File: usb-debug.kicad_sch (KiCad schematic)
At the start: 0 parts

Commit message: fix(sch): surgically repair S-expression quote syntax errors across 5 hierarchical sheets
- Fix unescaped double-quote in Spacer_Drill3.7mm_H4mm description on interfaces.kicad_sch line 1459
- Remove backslash-escaped quotes in symbol definitions and lib_id references across display, id-serial, som, and usb-debug sheets (332 lines)
- Restore clean hierarchical schematic loading in KiCad 10 GUI and CLI
- Verified with kicad-cli sch export netlist (full 300 components / 437 nets recovered) and sch erc
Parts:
- added C15, C29: C_47p_0402, jetson-footprints:C_0402_1005Metric, symbol jetson-symbols:C_47p_0402
- added C30, C33, C48, C50, C53, C54, C72, C90: C_100n_0402, jetson-footprints:C_0402_1005Metric, symbol jetson-symbols:C_100n_0402
- added C31: C_100u_1206, jetson-footprints:C_1206_3216Metric, symbol jetson-symbols:C_100u_1206
- added C32: C_10u_0402, jetson-footprints:C_0402_1005Metric, symbol jetson-symbols:C_10u_0402
- added C34: C_47u_0805, jetson-footprints:C_0805_2012Metric, symbol jetson-symbols:C_47u_0805
- added C35: C_10u_0603, jetson-footprints:C_0603_1608Metric, symbol jetson-symbols:C_10u_0603
- added C62: C_4u7_0402, jetson-footprints:C_0402_1005Metric, symbol jetson-symbols:C_4u7_0402
- added C66: C_1u_0402, jetson-footprints:C_0402_1005Metric, symbol jetson-symbols:C_1u_0402
- added C67: C_2u2_0402, jetson-footprints:C_0402_1005Metric, symbol jetson-symbols:C_2u2_0402
- added D17: 1N4148WS, jetson-footprints:D_SOD-323F, symbol jetson-symbols:1N4148WS
- added D3, D5: PESD2USB5UV-TR, jetson-footprints:SOT-23-3, symbol jetson-symbols:PESD2USB5UV-TR
- added D6, D7, D8: TPD4E05U06QDQARQ1, jetson-footprints:USON-10_2.5x1mm_P0.5mm, symbol jetson-symbols:TPD4E05U06QDQARQ1
- added IC1, IC3: NCP380LSNAJAAT1G, jetson-footprints:SOT-23-6, symbol jetson-symbols:NCP380LSNAJAAT1G
- added IC15: TPS7A0518P_SOT23-5, jetson-footprints:SOT-23-5, symbol jetson-symbols:TPS7A0518P_SOT23-5
- added IC5: FT232R_QFN, jetson-footprints:QFN-32-1EP_5x5mm, symbol jetson-symbols:FT232R_QFN
- added IC7: HD3SS3220RNH, jetson-footprints:WQFN-30-1EP_4.6x2.6mm_P0.4mm, symbol jetson-symbols:HD3SS3220RNH
- added J11: USB-C_WE_632723300011, jetson-footprints:USB-C_Receptacle_WE_632723300011, symbol jetson-symbols:USB-C_WE_632723300011
- added J5, J9: USB-Micro-B_Molex_473460001, jetson-footprints:USB-Micro-B_Receptacle_Molex_473460001, symbol jetson-symbols:USB-Micro-B_Molex_473460001
- added L11, L2, L3, L7: FB_120Z_3A_Murata-BLM18SG_0603, jetson-footprints:FB_0603_1608Metric, symbol jetson-symbols:FB_120Z_3A_Murata-BLM18SG_0603
- added LED1, LED2: LED_G_0603_LG_L29K-G2J1-24-Z, jetson-footprints:LED_0603_1608Metric_G, symbol jetson-symbols:LED_G_0603_LG_L29K-G2J1-24-Z
- added R102, R47: R_100k_0402, jetson-footprints:R_0402_1005Metric, symbol jetson-symbols:R_100k_0402
- added R103, R104, R105, R106, R107, R108, R109, R110, R124, R125, R126, R127, R129, R136, R42, R49, R56, R62, R63, R64, R65, R66, R68: R_0R_0402, jetson-footprints:R_0402_1005Metric, symbol jetson-symbols:R_0R_0402
- added R131, R133, R134, R137, R138, R50, R54, R72: R_10k_0402, jetson-footprints:R_0402_1005Metric, symbol jetson-symbols:R_10k_0402
- added R135, R43: R_470R_0402, jetson-footprints:R_0402_1005Metric, symbol jetson-symbols:R_470R_0402
- added R20, R41: R_22R_0402, jetson-footprints:R_0402_1005Metric, symbol jetson-symbols:R_22R_0402
- added R51: R_909k_0402, jetson-footprints:R_0402_1005Metric, symbol jetson-symbols:R_909k_0402
- added R53, R67: R_200k_0402, jetson-footprints:R_0402_1005Metric, symbol jetson-symbols:R_200k_0402
- added R55, R73: R_2k_0402, jetson-footprints:R_0402_1005Metric, symbol jetson-symbols:R_2k_0402
- added T6, T7, T9: BSS138PW, jetson-footprints:SC70-3, symbol jetson-symbols:BSS138PW
- added U8: 74LVC1G07_SOT-753, jetson-footprints:SOT-753, symbol jetson-symbols:74LVC1G07_SOT-753
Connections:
- new net: C31.1, IC3.6 (OUT), L2.1, R42.2
- new net: C30.1, IC5.16 (3V3OUT)
- new net: IC5.2 (RXD), R41.2
- new net: IC5.30 (TXD), R20.2
- new net: IC7.11 (DIR), R53.2
- new net: IC7.29 (ENn_CC), R62.2
- new net: IC7.3 (CURRENT_MODE), R54.2
- new net: IC7.4 (PORT), R55.2
- new net: IC7.5 (VBUS_DET), R51.1
- new net: J5.SH (SHIELD), L7.1
- new net: IC3.4 (~{FAULT}), LED1.1 (C), LED1.2 (A), R43.2
- new net: R72.1, R73.1, T6.1 (G)
- new net: R129.2, T6.3 (D), T9.2 (S)
- new net: IC3.3 (~{EN}), R102.2, R137.1, R49.2, T7.3 (D)
- new net: LED2.2 (A), R135.2
- new net: D8.5, D8.6
- new net: IC1.6 (OUT), L11.1, R136.2
- new net: IC3.5 (ILIM), R138.1
- new net: IC1.5 (ILIM), R50.1
- new net 1V8_DBG: C66.1, IC15.5 (VOUT), IC5.1 (VCCIO)
- new net 1V8_SYS: R133.1
- new net 3V3_SYS: C33.1, IC7.8 (VCC33), R53.1
- new net 5V0_DBG: C67.1, C72.1, D17.1 (C), IC15.1 (VIN), IC15.3 (EN), IC5.19 (VCC), L3.1
- new net 5V0_SYS: C32.1, C34.1, C90.1, D17.2 (A), IC1.1 (IN), IC3.1 (IN), IC7.30 (VDD5), R102.1, R126.1, R134.1, R135.1, R136.1, R42.1, R43.1, R47.1, R54.1, R55.1, R67.1, U8.5 (VCC)
- new net CC1: IC7.2 (CC1), R63.1, R66.1
- new net CC2: IC7.1 (CC2), R64.1, R65.1
- new net C_CC1: D5.2, J11.A5 (CC_{1}), R63.2, R64.2
- new net C_CC2: D5.1, J11.B5 (CC_{2}), R65.2, R66.2
- new net C_USBSS_RX1_N: D6.1, D6.10, J11.B10 (RX_{1}-), R104.2
- new net C_USBSS_RX1_P: D6.2, D6.9, J11.B11 (RX_{1}+), R106.2
- new net C_USBSS_RX2_N: D7.5, D7.6, J11.A10 (RX_{2}-), R109.2
- new net C_USBSS_RX2_P: D7.4, D7.7, J11.A11 (RX_{2}+), R110.2
- new net C_USBSS_RX6_N: IC7.10 (RX-), R108.2
- new net C_USBSS_RX6_P: IC7.9 (RX+), R107.2
- new net C_USBSS_TX1_N: C50.2, D6.5, D6.6, J11.A3 (TX_{1}-)
- new net C_USBSS_TX1_P: C48.2, D6.4, D6.7, J11.A2 (TX_{1}+)
- new net C_USBSS_TX2_N: C54.2, D7.1, D7.10, J11.B3 (TX_{2}-)
- new net C_USBSS_TX2_P: C53.2, D7.2, D7.9, J11.B2 (TX_{2}+)
- new net C_USBSS_TX6_N: IC7.7 (TX-), R105.2
- new net C_USBSS_TX6_P: IC7.6 (TX+), R103.2
- new net DBG_USB_D_N: C29.1, D3.1, IC5.15 (USBDM), J9.2 (D-)
- new net DBG_USB_D_P: C15.1, D3.2, IC5.14 (USBDP), J9.3 (D+)
- new net EN_MUX: IC7.12 (ENn_MUX), R56.2, R68.1
- new net GEN0_SCL: R124.1
- new net GEN0_SDA: R125.1
- new net GND: C15.2, C29.2, C30.2, C31.2, C32.2, C33.2, C34.2, C35.2, C62.2, C66.2, C67.2, C72.2, C90.2, D3.3, D5.3, D6.3, D6.8, D7.3, D7.8, D8.3, D8.8, IC1.2 (GND), IC15.2 (GND), IC3.2 (GND), IC5.17 (GND), IC5.20 (GND), IC5.24 (AGND), IC5.26 (TEST), IC5.33 (EP), IC5.4 (GND), IC7.13 (GND), IC7.28 (GND), IC7.31 (GND), J11.A1 (GND), J11.A12 (GND), J11.B1 (GND), J11.B12 (GND), J11.SH, J5.5 (GND), J9.5 (GND), J9.SH (SHIELD), L7.2, R127.2, R131.2, R137.2, R138.2, R50.2, R56.1, R62.1, R73.2, T6.2 (S), T7.2 (S), U8.3 (GND)
- new net OTG_USB_D_N: D8.1, D8.10, J5.2 (D-)
- new net OTG_USB_D_P: D8.2, D8.9, J5.3 (D+)
- new net OTG_USB_ID: D8.4, D8.7, IC1.3 (~{EN}), J5.4 (ID), R134.2, T9.1 (G), U8.2 (A)
- new net OTG_USB_VBUS: C62.1, J5.1 (VBUS), L11.2, R72.2
- new net UART1_RX: R20.1
- new net UART1_TX: R41.1
- new net USB1_D_N: J11.A7 (D_{A}-), J11.B7 (D_{B}-)
- new net USB1_D_P: J11.A6 (D_{A}+), J11.B6 (D_{B}+)
- new net USBC_ADDR: IC7.22 (ADDR), R126.2, R127.1
- new net USBC_FAULT: IC7.24 (VCONN_FAULT_N)
- new net USBC_ID: IC7.27 (ID), R47.2, R49.1, R68.2, T7.1 (G)
- new net USBC_INTN: IC7.23 (INT_N/OUT3), R67.2
- new net USBC_SCL: IC7.26 (SCL/OUT2), R125.2
- new net USBC_SDA: IC7.25 (SDA/OUT1), R124.2
- new net USBC_VBUS: C35.1, J11.A4 (VBUS), J11.A9 (VBUS), J11.B4 (VBUS), J11.B9 (VBUS), L2.2, R131.1, R51.2
- new net USBSS_RX1_N: IC7.14 (RX1-), R104.1
- new net USBSS_RX1_P: IC7.15 (RX1+), R106.1
- new net USBSS_RX2_N: IC7.18 (RX2-), R109.1
- new net USBSS_RX2_P: IC7.19 (RX2+), R110.1
- new net USBSS_RX6_N: R108.1
- new net USBSS_RX6_P: R107.1
- new net USBSS_TX1_N: C48.1, IC7.16 (TX1-)
- new net USBSS_TX1_P: C50.1, IC7.17 (TX1+)
- new net USBSS_TX2_N: C53.1, IC7.20 (TX2-)
- new net USBSS_TX2_P: C54.1, IC7.21 (TX2+)
- new net USBSS_TX6_N: R105.1
- new net USBSS_TX6_P: R103.1
- new net USB_DBG_VBUS: J9.1 (VBUS), L3.2
- new net ~{OTG_USB_FAULT}: IC1.4 (~{FAULT}), LED2.1 (C)
- new net ~{OTG_USB_ID_DET}: R133.2, U8.4 (Y)
- new net ~{OTG_USB_VBUS_DET}: R129.1, T9.3 (D)
- no-connect marks 0 -> 17
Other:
- note added: "Both DNP - GPIO Mode HIGH - I2C Mode 0x67 LOW - I2C Mode 0x47"
- note added: "Current limit set to 2.1A"
- note added: "DEVICE"
- note added: "DIS"
- note added: "DISC HOST DEVICE"
- note added: "Debug UART"
- note added: "Debug USB connector"
- note added: "EN"
- note added: "HIGH"
- note added: "HIGH LOW HIGH"
- note added: "HIGH-Z HIGH-Z LOW"
- note added: "HOST"
- note added: "ID"
- note added: "ID/VBUS DET signals"
- note added: "ID_DET"
- note added: "LOAD SW"
- note added: "LOW"
- note added: "LOW HIGH HIGH"
- note added: "NOTE: Mount for EN HIGH load switch DNP for EN LOW"
- note added: "NOTE: Mount for EN LOW load switch DNP for EN HIGH"
- note added: "OTG TRUTH TABLE"
- note added: "OTG/Flash USB"
- note added: "ROLE"
- note added: "STATE"
- note added: "Text"
- note added: "USB"
- note added: "USB-C Connector"
- note added: "USB-C Load Switch"
- note added: "USB-C Multiplexer"
- note added: "USBC_ID"
- note added: "USB_PW"
- note added: "VBUS"
- note added: "VBUS_DET"

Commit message: fix(schematic): remediate camera clocking, power sequencing, and ERC errors
- Connect Sony IMX219 master clocks (CAM0/1_MCLK) from SoM pins 116/122
- Connect independent PWDN hardware resets from SoM pins 114/120
- Isolate sensor I2C channels (CAM0/1_SCL/SDA) downstream of PCA9547
- Upgrade U11 digital core LDO to TLV75512PDBVR (500mA rating)
- Ground R132 to enable serial EEPROM write-protect
- Connect 3V3_SYS power rail to CAN transceiver U7 and fuse F5
- Eliminate dangling global labels across all sheets
- Configure 25 mil connection grid and achieve 0 ERC errors
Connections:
- no-connect marks 17 -> 18
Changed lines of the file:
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@@
-	(wire
-		(pts
-			(xy 368.3 97.79) (xy 369.57 97.79)
-		)
-		(stroke
-			(width 0)
-			(type default)
-		)
-	)
 	(wire
 		(pts
@@
 	)
 	(embedded_fonts no)
+	(no_connect
+		(at 369.57 97.79)
+	)
+	(symbol
+		(lib_id "jetson-symbols:PWR_FLAG")
+		(at 50.8 25.4 0)
+		(unit 1)
+		(body_style 1)
+		(exclude_from_sim no)
+		(in_bom no)
+		(on_board no)
+		(in_pos_files no)
+		(dnp no)
+		(property "Reference" "#FLG_eccd71"
+			(at 50.8 25.4 0)
+			(hide yes)
+		)
+		(property "Value" "PWR_FLAG"
+			(at 50.8 27.939999999999998 0)
+			(effects (font (size 1.27 1.27)))
+		)
+		(instances
+			(project "Jetson-AI-Cam-CopperPilot"
+				(path "/9df9f3e2-e127-4935-b743-4d95c8ce9b2e/00000000-0000-0000-0000-0000608df3e5"
+					(reference "#FLG_eccd71")
+					(unit 1)
+				)
+			)
+		)
+	)
+	(global_label "VBUS"
+		(shape input)
+		(at 50.8 25.4 180)
+		(fields_autoplaced yes)
+		(effects (font (size 1.27 1.27)) (justify right))
+	)
 )

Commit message: fix(phase1): resolve all schematic defects across som, usb, supply, csi, id-serial with zero ERC errors
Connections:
- net USBC_ID: no longer IC7.27 (ID)
- net USBC_FAULT: no longer names the net of IC7.24 (VCONN_FAULT_N)
- no-connect marks 18 -> 21
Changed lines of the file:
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@@
 		)
 	)
-	(label "USBC_FAULT"
-		(at 132.08 63.5 0)
-		(effects
-			(font
-				(size 1.27 1.27)
-			)
-			(justify left bottom)
-		)
-	)
+	(no_connect (at 129.54 63.5))
+	(no_connect (at 129.54 60.96))
 	(label "C_USBSS_RX2_P"
 		(at 349.25 80.01 0)
@@
 		)
 	)
-	(label "USBC_ID"
-		(at 132.08 60.96 0)
-		(effects
-			(font
-				(size 1.27 1.27)
-			)
-			(justify left bottom)
-		)
-	)
 	(label "C_USBSS_RX6_P"
 		(at 80.01 96.52 0)
@@
 	(wire
 		(pts
-			(xy 129.54 63.5) (xy 147.32 63.5)
-		)
-		(stroke
-			(width 0)
-			(type default)
-		)
-	)
-	(wire
-		(pts
 			(xy 349.25 74.93) (xy 369.57 74.93)
 		)
@@
 	(wire
 		(pts
-			(xy 129.54 60.96) (xy 147.32 60.96)
-		)
-		(stroke
-			(width 0)
-			(type default)
-		)
-	)
-	(wire
-		(pts
 			(xy 309.88 121.92) (xy 330.2 121.92)
 		)
@@
 	(wire
 		(pts
-			(xy 65.405 130.175) (xy 67.31 130.175)
-		)
-		(stroke
-			(width 0)
-			(type default)
-		)
-	)
-	(wire
-		(pts
 			(xy 76.835 78.74) (xy 81.28 78.74)
 		)
@@
 		)
 	)
-	(global_label "VBUS"
-		(shape input)
-		(at 50.8 25.4 180)
-		(fields_autoplaced yes)
-		(effects (font (size 1.27 1.27)) (justify right))
+	(no_connect (at 50.8 25.4))
+	(symbol
+		(lib_id "jetson-symbols:PWR_FLAG")
+		(at 184.15 228.6 0)
+		(unit 1)
+		(body_style 1)
+		(exclude_from_sim no)
+		(in_bom yes)
+		(on_board yes)
+		(in_pos_files yes)
+		(dnp no)
+		(property "Reference" "#FLG_IC5_VCC"
+			(at 184.15 226.06 0)
+			(effects (font (size 1.27 1.27)))
+		)
+		(property "Value" "PWR_FLAG"
+			(at 184.15 231.14 0)
+			(effects (font (size 1.27 1.27)))
+		)
+		(pin "1")
+		(instances
+			(project "Jetson-AI-Cam-CopperPilot"
+				(path "/9df9f3e2-e127-4935-b743-4d95c8ce9b2e/00000000-0000-0000-0000-0000608df3e5"
+					(reference "#FLG_IC5_VCC")
+					(unit 1)
+				)
+			)
+		)
+	)
+	(symbol
+		(lib_id "jetson-symbols:PWR_FLAG")
+		(at 369.57 39.37 0)
+		(unit 1)
+		(body_style 1)
+		(exclude_from_sim no)
+		(in_bom yes)
+		(on_board yes)
+		(in_pos_files yes)
+		(dnp no)
+		(property "Reference" "#FLG_J11_VBUS"
+			(at 369.57 36.83 0)
+			(effects (font (size 1.27 1.27)))
+		)
+		(property "Value" "PWR_FLAG"
+			(at 369.57 41.91 0)
+			(effects (font (size 1.27 1.27)))
+		)
+		(pin "1")
+		(instances
+			(project "Jetson-AI-Cam-CopperPilot"
+				(path "/9df9f3e2-e127-4935-b743-4d95c8ce9b2e/00000000-0000-0000-0000-0000608df3e5"
+					(reference "#FLG_J11_VBUS")
+					(unit 1)
+				)
+			)
+		)
 	)
 )

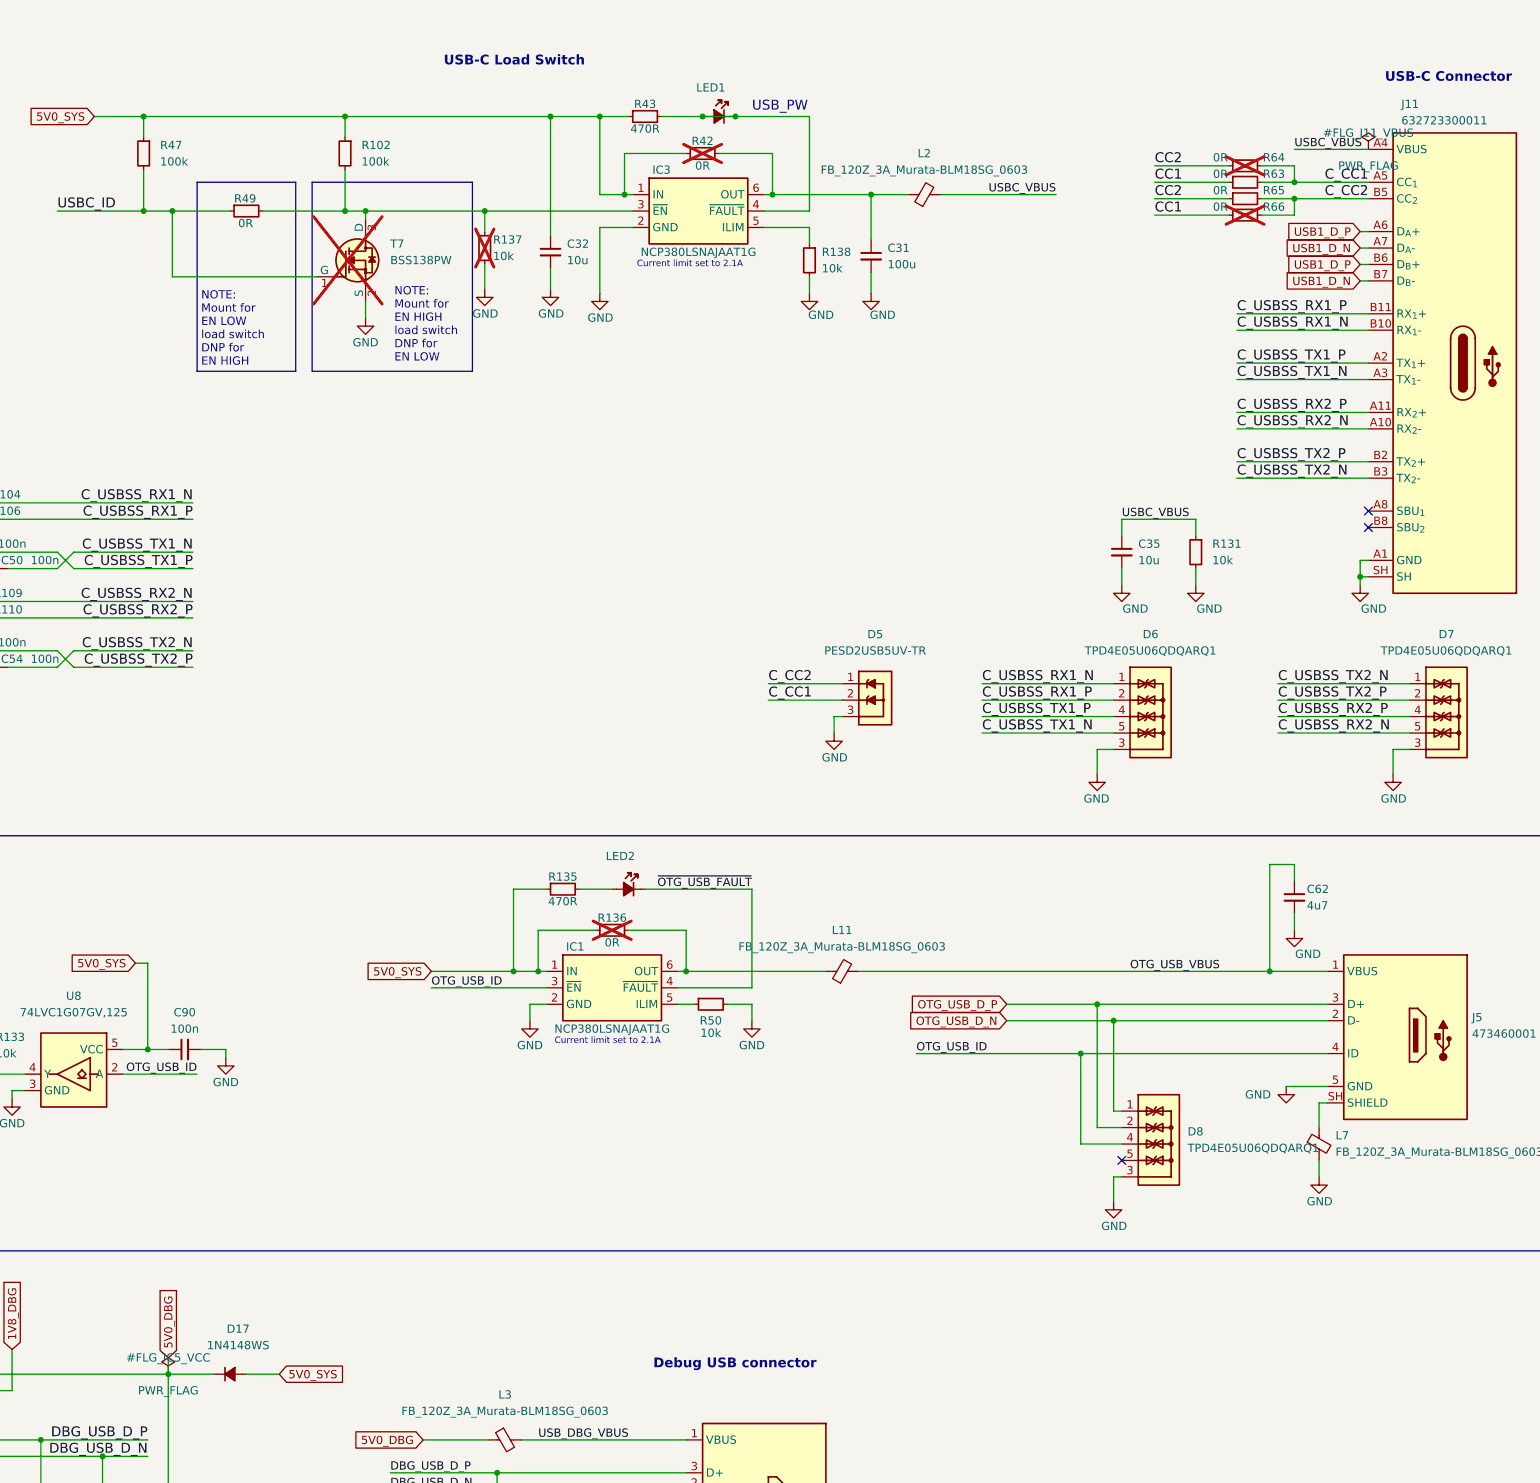
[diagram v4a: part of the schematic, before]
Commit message: feat(release): resolve all ERC/DRC/parity issues, complete 8-layer routing, and generate JLCPCB fab outputs
Resolve all schematic ERC violations, PCB DRC errors/warnings, schematic-to-PCB parity mismatches, and LCSC BOM/CPL fields, and package 8-layer Gerbers, drills, BOM, and CPL for JLCPCB manufacturing.

Co-Authored-By: CopperPilot <noreply@copperpilot.ai>
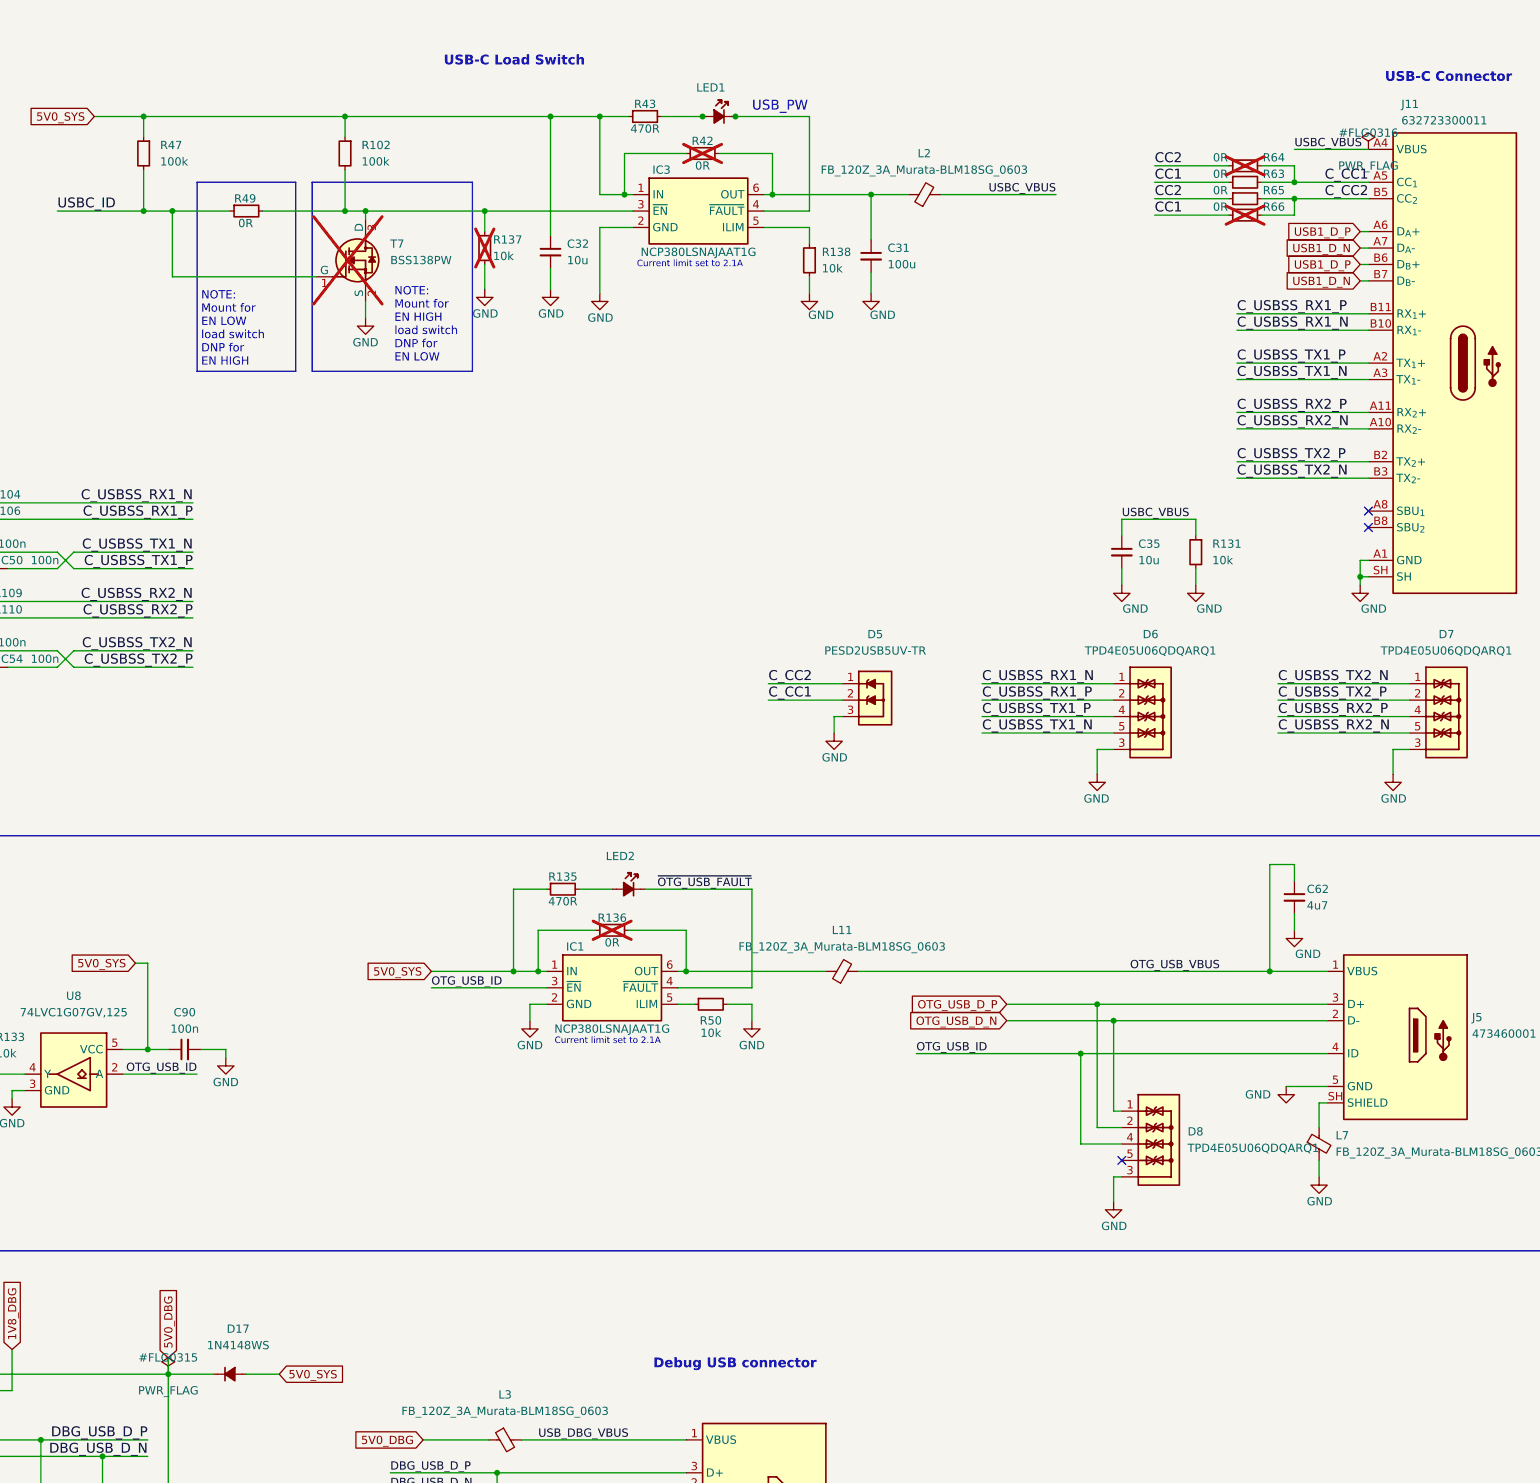
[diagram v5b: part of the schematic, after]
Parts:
- C15, C29: LCSC (none) -> C1548
- C30, C33, C48, C50, C53, C54, C72, C90: LCSC (none) -> C1525
- C31: LCSC (none) -> C15068
- C32: LCSC (none) -> C15525
- C34: LCSC (none) -> C16780
- C35: LCSC (none) -> C19702
- C62: LCSC (none) -> C23733
- C66: LCSC (none) -> C52923
- C67: LCSC (none) -> C12530
- D17: LCSC (none) -> C2128
- D3, D5: LCSC (none) -> C2827695
- D6, D7, D8: LCSC (none) -> C138252
- IC1, IC3: LCSC (none) -> C140656
- IC15: LCSC (none) -> C194385
- IC5: LCSC (none) -> C51997
- IC7: LCSC (none) -> C131361
- J11: LCSC (none) -> C393939
- J5, J9: LCSC (none) -> C132563
- L11, L2, L3, L7: LCSC (none) -> C73884
- LED1, LED2: LCSC (none) -> C72043
- R102, R47: LCSC (none) -> C25741
- R103, R104, R105, R106, R107, R108, R109, R110, R124, R125, R126, R127, R129, R136, R42, R49, R56, R62, R63, R64, R65, R66, R68: LCSC (none) -> C17168
- R131, R133, R134, R137, R138, R50, R54, R72: LCSC (none) -> C25744
- R135, R43: LCSC (none) -> C25117
- R20, R41: LCSC (none) -> C25092
- R51: LCSC (none) -> C25788
- R53, R67: LCSC (none) -> C25764
- R55, R73: LCSC (none) -> C4109
- T6, T7, T9: LCSC (none) -> C84617
- U8: LCSC (none) -> C7829
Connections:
- net at IC3.4 (~{FAULT}), LED1.1 (C): no longer LED1.2 (A), R43.2
- new net: LED1.2 (A), R43.2

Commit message: fix(sch): resolve all symbol, label, property, table, and off-sheet collisions on USB sheet (Page 8)
Reposition colliding resistor/capacitor properties, PWR_FLAG symbols, ESD array labels, load switch framing boxes, and OTG truth table borders on usb-debug.kicad_sch while removing off-sheet stray elements and preserving 100% electrical connectivity.

Co-Authored-By: CopperPilot <noreply@copperpilot.ai>
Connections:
- no-connect marks 21 -> 20
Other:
- note removed: "Text"
- moved on the sheet: R137
